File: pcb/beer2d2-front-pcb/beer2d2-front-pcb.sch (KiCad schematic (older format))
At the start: 18 parts

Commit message: first pass at board layout. will probably try again
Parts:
- removed C?: 10uF, ~, symbol C
- removed C?: 1uF, ~, symbol C
- added C7: 0.1uF, ~, symbol C_POL
- added C8: 0.33uF, ~, symbol C_POL
- gave numbers to parts that had none: 16
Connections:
- net VLED is gone; now on net VCC: J1.2, J2.2, J3.2, J4.2
- net GND: now also C7.2, C8.2
- net TLC_SCK: now also IC1.27 (PC4(ADC4/SDA/PCINT12)); no longer IC1.28 (PC5(ADC5/SCL/PCINT13))
- net TLC_SDA: now also IC1.28 (PC5(ADC5/SCL/PCINT13)); no longer IC1.27 (PC4(ADC4/SDA/PCINT12))
- net VCC: now also C7.1
- net VIN: now also C8.1
- net C6: now reaches IC1.7 (XTAL1(PB6))
- net COL0 renamed C0
- net COL1 renamed C1
- net COL2 renamed C2
- net ROW0 renamed R0
- net ROW1 renamed R1
- net ROW2 renamed R2
- net ROW3 renamed R3
- net ROW4 renamed R4
- net ROW5 renamed R5
- net ROW6 renamed R6
- net ROW7 renamed R7
- no-connect marks 10 -> 9

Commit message: liking this placement a lot more
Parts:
- removed C6: 0.1uF, ~, symbol C
- IC2: value VCC_REG -> 5VREG
- IC3: value TLC5971_SOP -> TLC5971
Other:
- moved on the sheet: C5
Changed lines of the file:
@@
 P 8800 2100
 F 0 "IC3" H 8600 2950 60  0000 C CNN
-F 1 "TLC5971_SOP" H 8800 2850 60  0000 C CNN
+F 1 "TLC5971" H 8800 2850 60  0000 C CNN
 F 2 "~" H 8800 2100 60  0001 C CNN
 F 3 "~" H 8800 2100 60  0001 C CNN
@@
 	8200 2150 8300 2150
 $Comp
-L C C6
-U 1 1 52818818
-P 8000 1750
-F 0 "C6" H 8600 1750 60  0000 C CNN
-F 1 "0.1uF" H 8350 1750 60  0000 C CNN
-F 2 "~" H 8000 1750 60  0001 C CNN
-F 3 "~" H 8000 1750 60  0001 C CNN
-	1    8000 1750
-	-1   0    0    1
-$EndComp
-$Comp
 L GND #PWR05
 U 1 1 5281885E
@@
 	0    1    1    0
 $EndComp
-$Comp
-L C C5
-U 1 1 5281886D
-P 8000 1550
-F 0 "C5" H 7400 1550 60  0000 C CNN
-F 1 "1uF" H 7700 1550 60  0000 C CNN
-F 2 "~" H 8000 1550 60  0001 C CNN
-F 3 "~" H 8000 1550 60  0001 C CNN
-	1    8000 1550
-	1    0    0    -1
-$EndComp
 Wire Wire Line
 	7800 1950 8300 1950
-Wire Wire Line
-	7850 1550 7850 1950
-Wire Wire Line
-	7850 1550 7900 1550
-Wire Wire Line
-	7850 1750 7900 1750
-Connection ~ 7850 1750
-Connection ~ 7850 1950
-Wire Wire Line
-	8100 1750 8300 1750
-Wire Wire Line
-	8100 1550 8300 1550
 $Comp
 L VCC #PWR06
@@
 Wire Wire Line
 	8200 1500 8200 1750
-Connection ~ 8200 1550
 Connection ~ 8200 1750
 $Comp
@@
 P 7700 5950
 F 0 "IC2" H 7600 6150 60  0000 C CNN
-F 1 "VCC_REG" H 7700 5750 60  0000 C CNN
+F 1 "5VREG" H 7700 5750 60  0000 C CNN
 F 2 "~" H 7700 5950 60  0000 C CNN
 F 3 "~" H 7700 5950 60  0000 C CNN
@@
 Wire Wire Line
 	7950 2900 7550 2900
+$Comp
+L C C5
+U 1 1 5281886D
+P 8200 1850
+F 0 "C5" V 8250 2050 60  0000 C CNN
+F 1 "1uF" V 8150 2050 60  0000 C CNN
+F 2 "~" H 8200 1850 60  0001 C CNN
+F 3 "~" H 8200 1850 60  0001 C CNN
+	1    8200 1850
+	0    -1   -1   0
+$EndComp
+Connection ~ 8200 1950
+Wire Wire Line
+	8200 1750 8300 1750
+Wire Wire Line
+	8200 1550 8300 1550
+Connection ~ 8200 1550
 $EndSCHEMATC

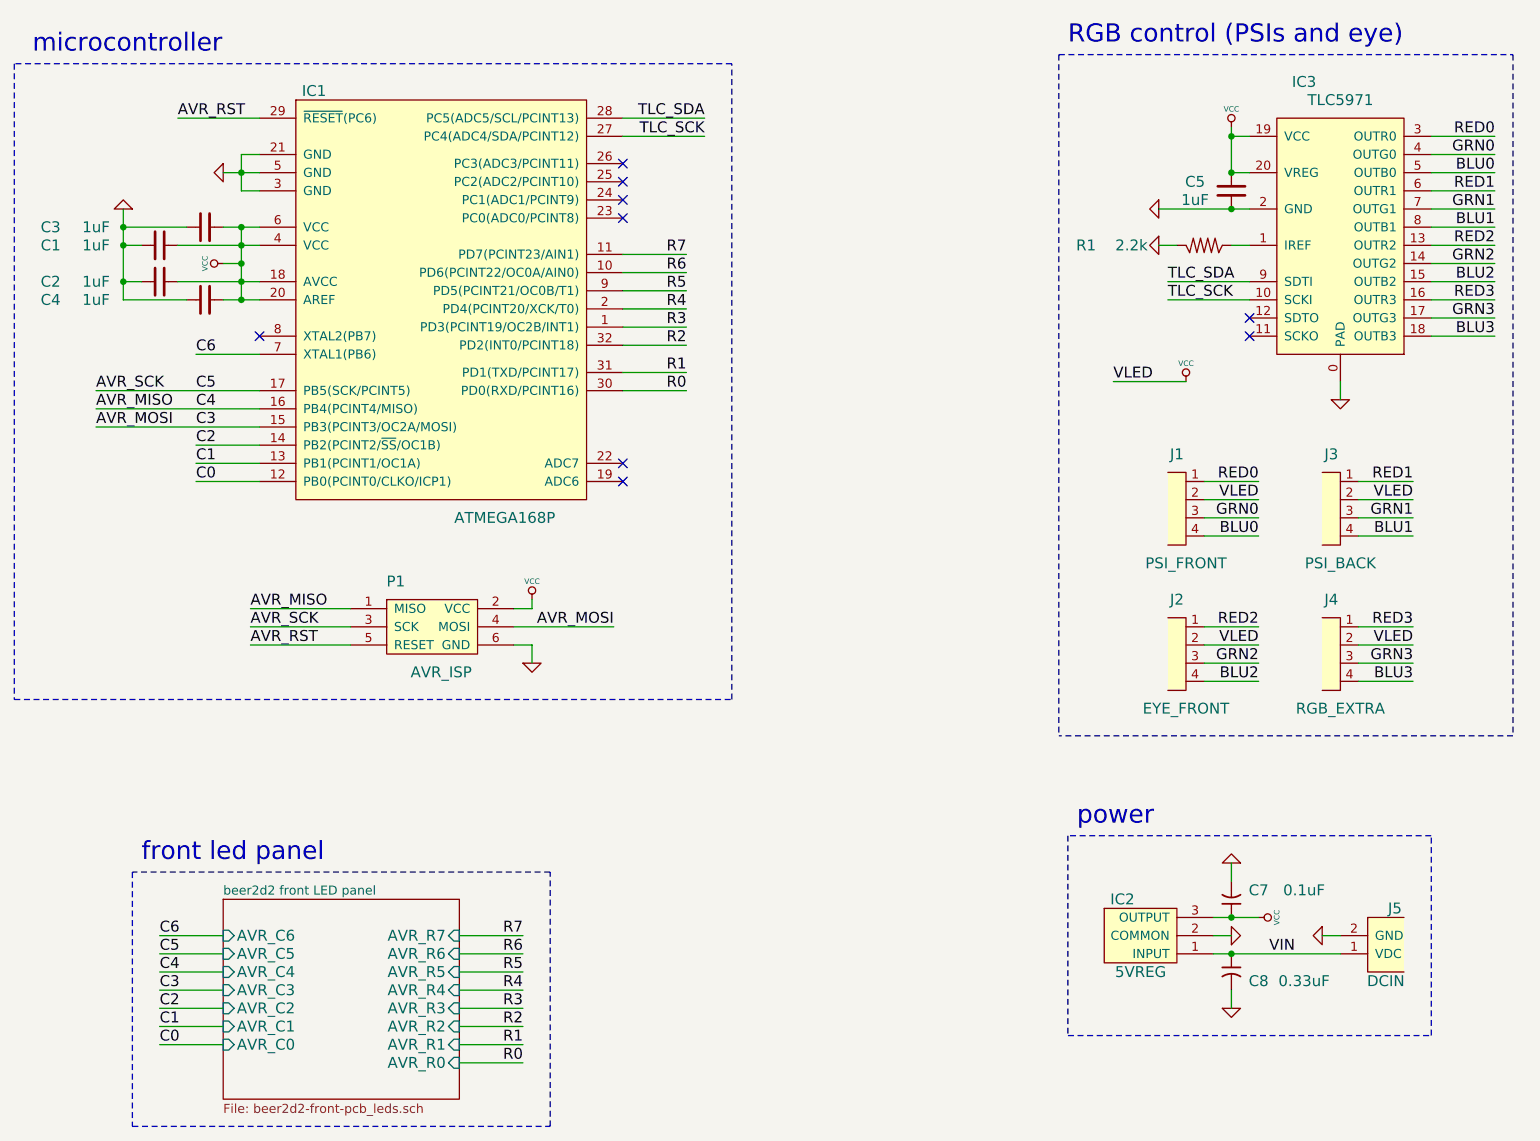
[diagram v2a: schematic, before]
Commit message: redoing front board
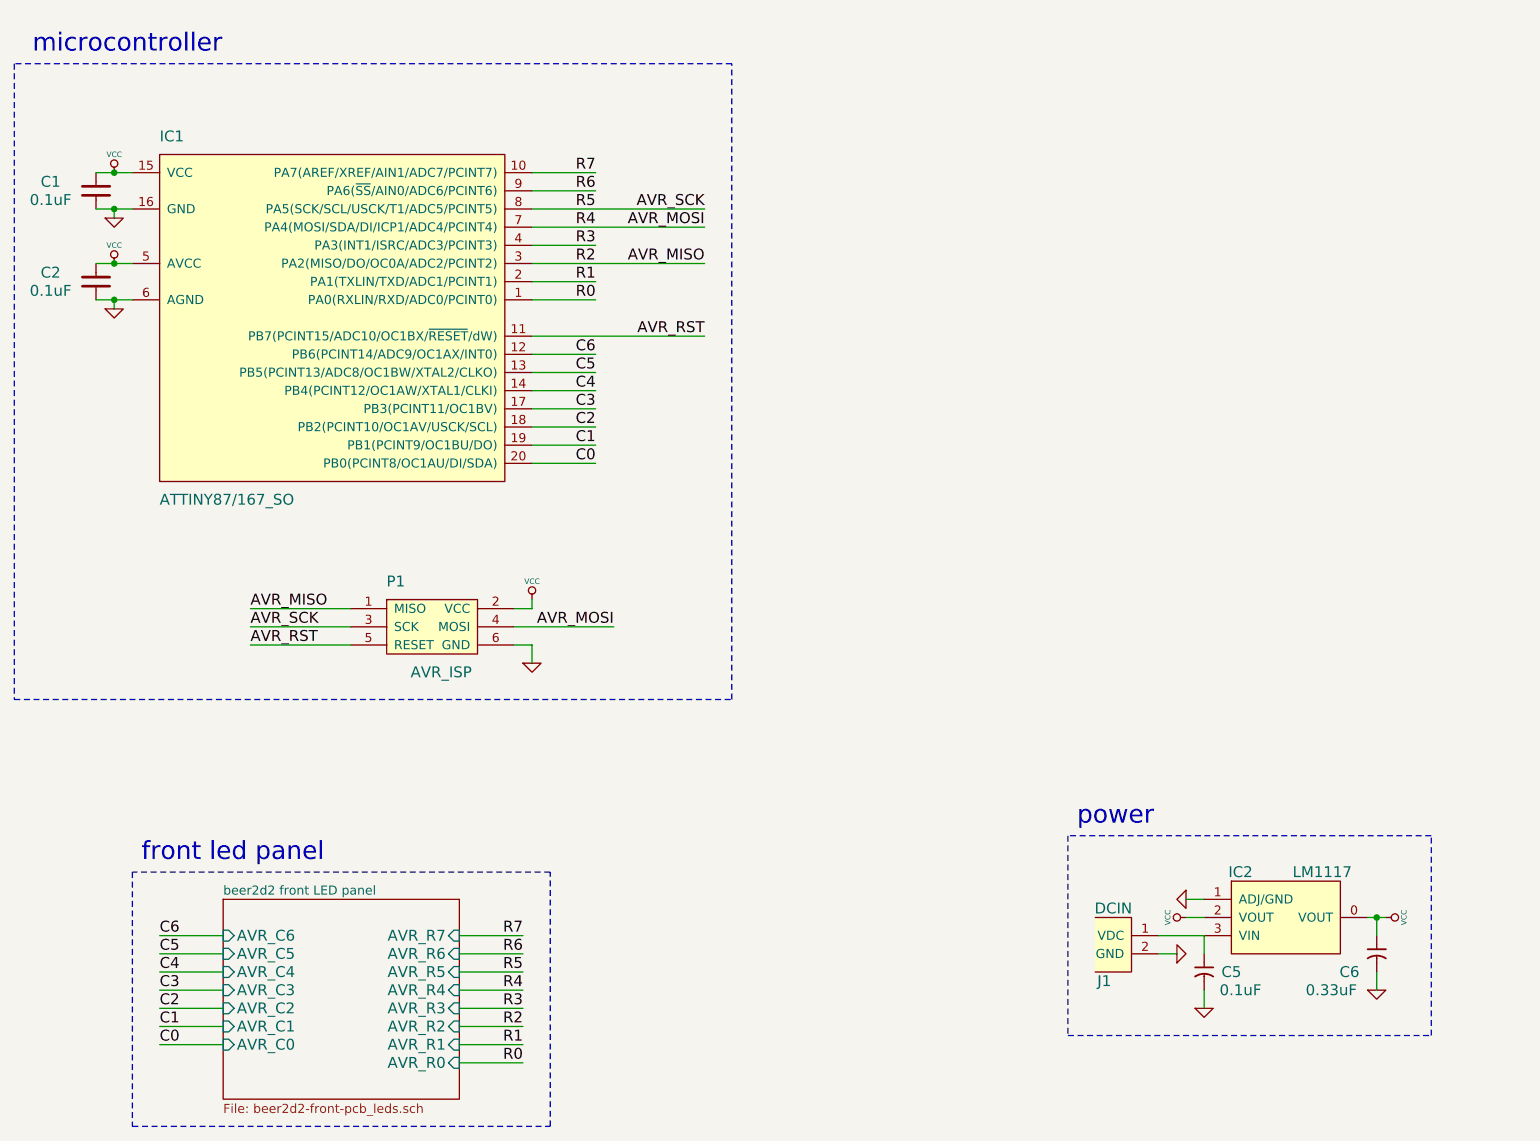
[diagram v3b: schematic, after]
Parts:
- removed C3, C4, C5: 1uF, ~, symbol C
- removed IC1: ATMEGA168P, ~, symbol ATMEGA328P_TQFP
- removed IC2: 5VREG, ~, symbol VCC_REG
- removed IC3: TLC5971, ~, symbol TLC5971_SOP
- removed J1: PSI_FRONT, ~, symbol 4PIN_FEMALE
- removed J2: EYE_FRONT, ~, symbol 4PIN_FEMALE
- removed J3: PSI_BACK, ~, symbol 4PIN_FEMALE
- removed J4: RGB_EXTRA, ~, symbol 4PIN_FEMALE
- removed R1: 2.2k, ~, symbol R
- added IC1: ATTINY87/167_SO, ~, symbol ATTINY87/167_SO
- added IC2: LM1117, ~, symbol LM1117
- C1, C2: value 1uF -> 0.1uF
- renumbered C7 to C5, C8 to C6, J5 to J1
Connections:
- net AVR_MISO: now also IC1.3 (PA2(MISO/DO/OC0A/ADC2/PCINT2))
- net AVR_MOSI: now also IC1.7 (PA4(MOSI/SDA/DI/ICP1/ADC4/PCINT4))
- net AVR_RST: now also IC1.11 (PB7(PCINT15/ADC10/OC1BX/~RESET~/dW))
- net AVR_SCK: now also IC1.8 (PA5(SCK/SCL/USCK/T1/ADC5/PCINT5))
- net C0: now also IC1.20 (PB0(PCINT8/OC1AU/DI/SDA))
- net C1: now also IC1.19 (PB1(PCINT9/OC1BU/DO))
- net C2: now also IC1.18 (PB2(PCINT10/OC1AV/USCK/SCL))
- net C6: now also IC1.12 (PB6(PCINT14/ADC9/OC1AX/INT0))
- net GND: now also IC1.16 (GND), IC1.6 (AGND), IC2.1 (ADJ/GND)
- net R0: now also IC1.1 (PA0(RXLIN/RXD/ADC0/PCINT0))
- net R1: now also IC1.2 (PA1(TXLIN/TXD/ADC1/PCINT1))
- net R3: now also IC1.4 (PA3(INT1/ISRC/ADC3/PCINT3))
- net R6: now also IC1.9 (PA6(~SS~/AIN0/ADC6/PCINT6))
- net R7: now also IC1.10 (PA7(AREF/XREF/AIN1/ADC7/PCINT7))
- net VCC: now also C6.1, IC1.15 (VCC), IC1.5 (AVCC), IC2.0 (VOUT), IC2.2 (VOUT); no longer C5.1
- net VIN: no longer names the net of J1.1 (VDC)
- net VIN: now also C5.1, IC2.3 (VIN); no longer C6.1
- new net C3: IC1.17 (PB3(PCINT11/OC1BV))
- new net C4: IC1.14 (PB4(PCINT12/OC1AW/XTAL1/CLKI))
- new net C5: IC1.13 (PB5(PCINT13/ADC8/OC1BW/XTAL2/CLKO))
- no-connect marks 9 -> 0
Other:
- note removed: "RGB control (PSIs and eye)"
- moved on the sheet: C1, C2, C5, C6, J1

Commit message: layout complete
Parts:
- IC1: value ATTINY87/167_SO -> ATTINY167
- J1: value DCIN -> 6-12V
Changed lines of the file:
@@
 Sheet 1 2
 Title "beer2d2 (working title) head control"
-Date "22 jan 2014"
+Date "23 jan 2014"
 Rev "0.1"
 Comp "Wiley Cousins, LLC."
@@
 P 7550 6000
 F 0 "J1" H 7500 5800 60  0000 C CNN
-F 1 "DCIN" H 7550 6200 60  0000 C CNN
+F 1 "6-12V" H 7550 6200 60  0000 C CNN
 F 2 "~" H 7550 6000 60  0000 C CNN
 F 3 "~" H 7550 6000 60  0000 C CNN
@@
 P 3250 2550
 F 0 "IC1" H 2300 3550 60  0000 L CNN
-F 1 "ATTINY87/167_SO" H 2300 1550 60  0000 L CNN
+F 1 "ATTINY167" H 2300 1550 60  0000 L CNN
 F 2 "~" H 2300 3250 60  0001 C CNN
 F 3 "~" H 3000 2550 60  0001 C CNN

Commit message: moving on to rear pcb
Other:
- note added: "front led panel (page 2)"
- note removed: "front led panel"
- moved on the sheet: C1, C2, C5, C6, IC1, IC2, J1, P1
